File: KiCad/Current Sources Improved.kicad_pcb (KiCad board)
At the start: 4 copper layers, 120 x 75 mm, 97 parts, among them J201 OUT+, J202 OUT-, J203 V+, J204 V-, J301 AVR-ISP-6, J302 USB B, Q201 IRF510, Q401 FMMT614TA, Q402 FMMT734, U201 ADR441, U202 LTC1595, U203 OPA4182, U204 AD7791, U205 ORNTA1001AT1, U301 FT231XS-U, U302 ATMEGA328P-AUR, U303 ADuM261, U304 TMP117xxDRV, U401 L78L15_SOT89, U402 PESE1-S5-S24-M, U403 L78L05, U404 L79L15_SOT89, Y301 16 MHz

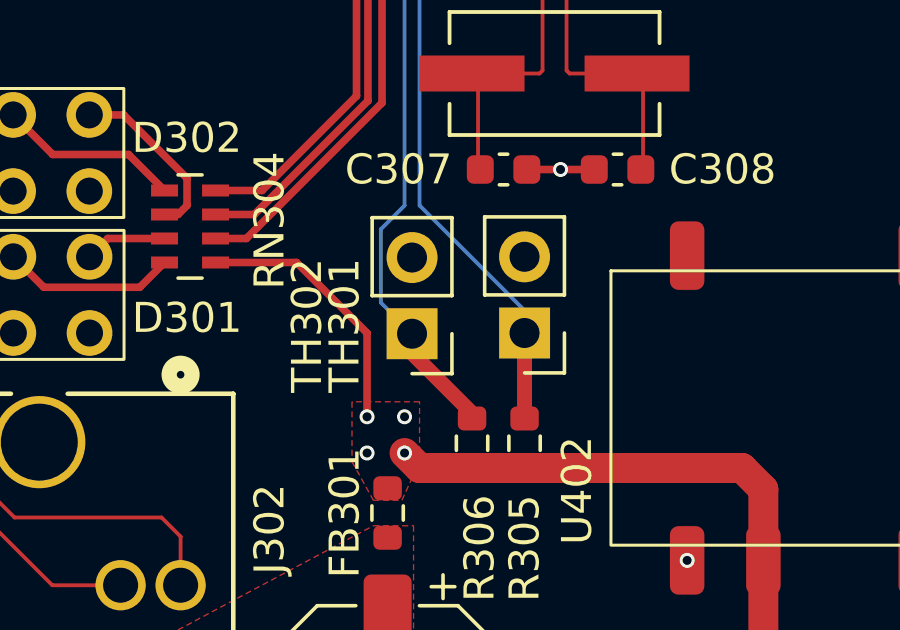
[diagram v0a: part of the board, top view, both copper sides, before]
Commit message: Adjusted designators for NTCs
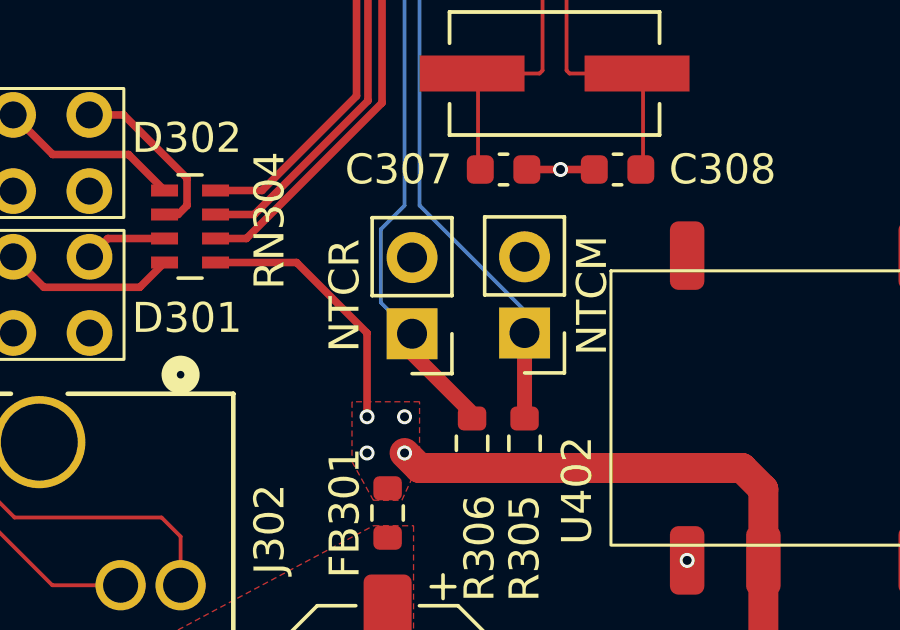
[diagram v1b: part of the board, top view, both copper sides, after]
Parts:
- renumbered TH301 to NTCM, TH302 to NTCR
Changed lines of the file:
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@@
       (drillshape 0)
       (scaleselection 1)
-      (outputdirectory "Z:/Current Sources Improved/Gerbers/")
+      (outputdirectory "Z:/Precision Current Source/KiCad/Gerbers/")
     )
   )
@@
     (property "ki_keywords" "R res thermistor")
     (attr through_hole)
-    (fp_text reference "TH302" (at 3.5 0.275 90) (layer "F.SilkS")
+    (fp_text reference "NTCR" (at 2.25 1.275 90) (layer "F.SilkS")
         (effects (font (size 1 1) (thickness 0.15)))
     )
@@
     (property "ki_keywords" "R res thermistor")
     (attr through_hole)
-    (fp_text reference "TH301" (at 6 0.25 270) (layer "F.SilkS")
+    (fp_text reference "NTCM" (at -2.25 1.25 270) (layer "F.SilkS")
         (effects (font (size 1 1) (thickness 0.15)))
     )
@@
     (effects (font (size 1 1) (thickness 0.15)) (justify left bottom))
   )
-  (gr_text locked "M MORANO\nREV 2.0\n11/27/24" (at 81.5 72) (layer "F.SilkS")
+  (gr_text locked "M MORANO\nREV 2.0\n4/28/25" (at 81.5 72) (layer "F.SilkS")
     (effects (font (size 1 1) (thickness 0.2) bold) (justify left bottom))
   )

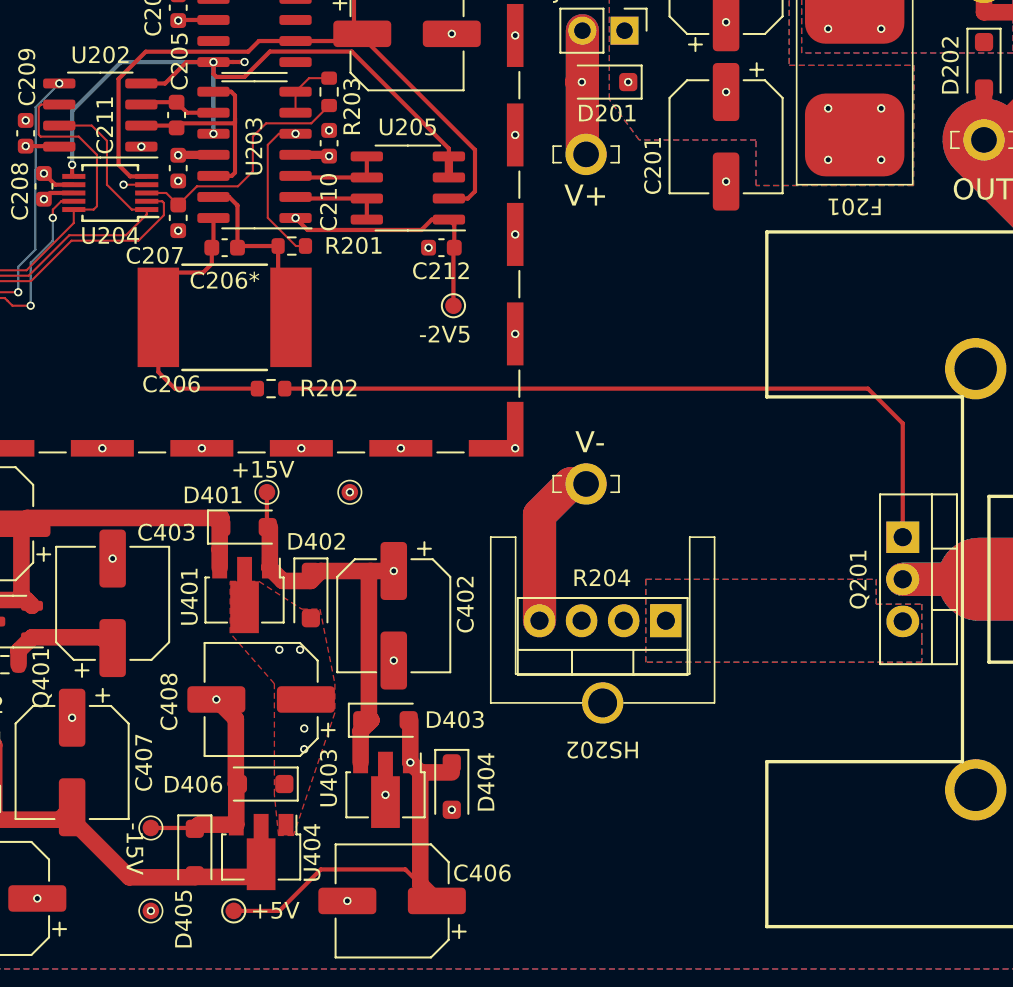
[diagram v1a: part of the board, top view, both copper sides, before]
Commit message: Updated some designators and added component list
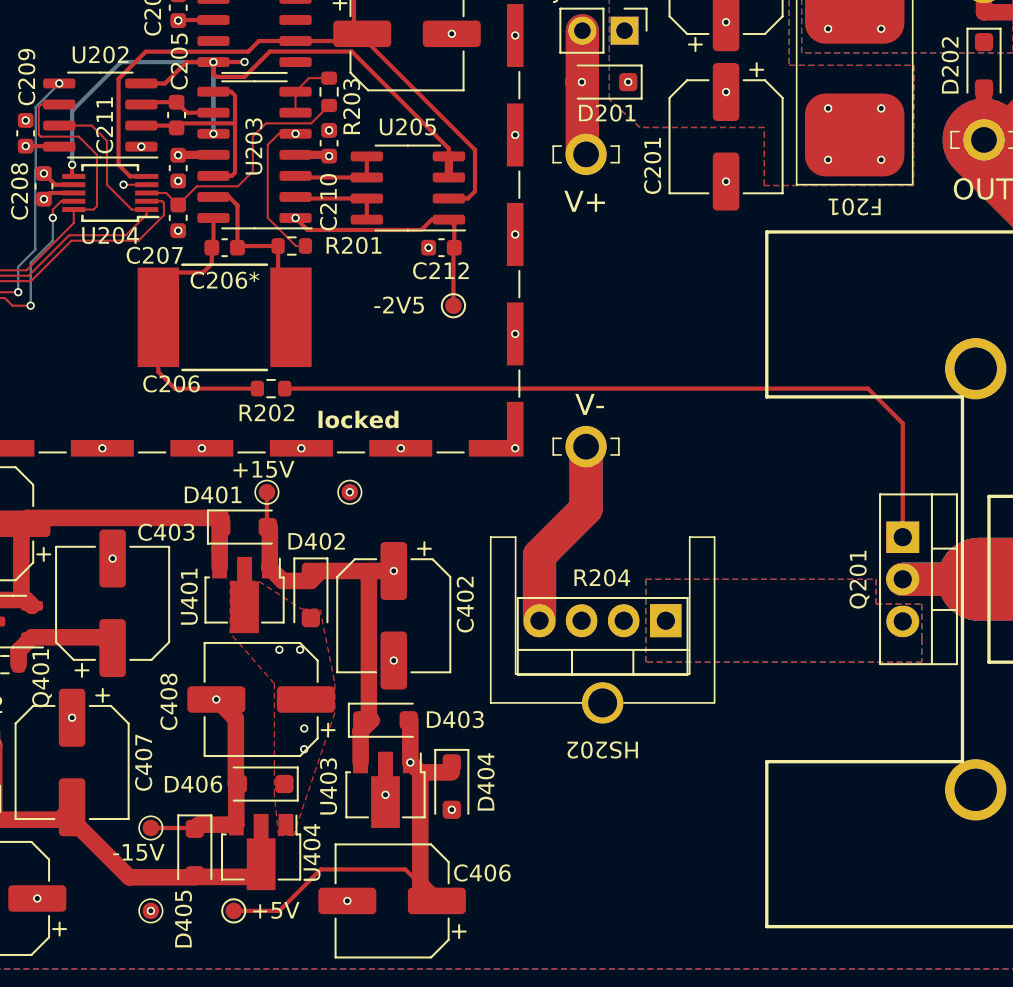
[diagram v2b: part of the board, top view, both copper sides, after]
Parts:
- moved J204 2.25 mm to (162.0, 98.5)
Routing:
- net GNDA: track 28.1 -> 31.5 mm
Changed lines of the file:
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@@
         (effects (font (size 1 1) (thickness 0.1)))
     )
-    (fp_text value "-15V" (at -1.25 1 -90 unlocked) (layer "F.SilkS")
+    (fp_text value "-15V" (at -1 0.75 unlocked) (layer "F.SilkS")
         (effects (font (size 1 1) (thickness 0.15)))
     )
@@
         (effects (font (size 1 1) (thickness 0.15)))
     )
-    (fp_text value "-2V5" (at -0.5 1.75) (layer "F.SilkS")
+    (fp_text value "-2V5" (at -3.25 0) (layer "F.SilkS")
         (effects (font (size 1 1) (thickness 0.15)))
     )
@@
     (property "ki_keywords" "Voltage Regulator 100mA Positive")
     (attr smd)
-    (fp_text reference "U403" (at -1 3.4 90) (layer "F.SilkS")
+    (fp_text reference "U403" (at -0.5 3.4 90) (layer "F.SilkS")
         (effects (font (size 1 1) (thickness 0.15)))
     )
@@
   )
   (footprint "Components:1211" locked (layer "F.Cu")
-    (at 162 100.75 180)
+    (at 162 98.5 180)
     (descr "1211-1")
     (tags "Undefined or Miscellaneous")
@@
         (effects (font (size 1.27 1.27) (thickness 0.254)))
     )
-    (fp_text value "V+" (at 0 2.5) (layer "F.SilkS")
+    (fp_text value "V+" (at 0 2.877596) (layer "F.SilkS")
         (effects (font (size 1.27 1.27) (thickness 0.254)))
     )
@@
     (property "ki_keywords" "R res resistor")
     (attr smd)
-    (fp_text reference "R202" (at 3.5 0) (layer "F.SilkS")
+    (fp_text reference "R202" (at -0.25 1.5) (layer "F.SilkS")
         (effects (font (size 1 1) (thickness 0.15)))
     )
@@
     (effects (font (size 1 1) (thickness 0.2) bold) (justify left bottom))
   )
+  (gr_text locked "DO NOT \nPOPUPLATE\nC206* IF \nUSING C206" (at 145.75 97.5) (layer "F.SilkS")
+    (effects (font (size 1 1) (thickness 0.2) bold) (justify left bottom))
+  )
   (gr_text locked "MOSI" (at 101.75 80.5 90) (layer "F.SilkS")
     (effects (font (size 1 1) (thickness 0.15)) (justify left bottom))
@@
     (style (thickness 0.15) (arrow_length 1.27) (text_position_mode 0) (extension_height 0.58642) (extension_offset 0.5) keep_text_aligned)
   )
+  (segment locked (start 159.19 105.06) (end 159.19 109) (width 2) (layer "F.Cu") (net 1))
   (segment locked (start 141.4 75.3) (end 141.1 75.3) (width 0.254) (layer "F.Cu") (net 1))
-  (segment locked (start 162 100.75) (end 161.05 100.75) (width 2) (layer "F.Cu") (net 1))
-  (segment locked (start 159.19 102.61) (end 159.19 109) (width 2) (layer "F.Cu") (net 1))
-  (segment locked (start 161.05 100.75) (end 159.19 102.61) (width 2) (layer "F.Cu") (net 1))
+  (segment locked (start 162 98.5) (end 162 102.25) (width 2) (layer "F.Cu") (net 1))
+  (segment locked (start 162 102.25) (end 159.19 105.06) (width 2) (layer "F.Cu") (net 1))
   (segment locked (start 129.975 82.7) (end 131.1 82.7) (width 0.254) (layer "F.Cu") (net 1))
   (segment locked (start 119.3 98.7) (end 119.3 99.90625) (width 1) (layer "F.Cu") (net 1))
@@
   (via locked (at 114.54 119.83) (size 0.5) (drill 0.3) (layers "F.Cu" "B.Cu") (net 1))
   (via locked (at 157.725 66.8) (size 0.5) (drill 0.3) (layers "F.Cu" "B.Cu") (net 1))
-  (segment locked (start 161.05 100.75) (end 159.19 102.61) (width 2) (layer "B.Cu") (net 1))
-  (segment locked (start 162 100.75) (end 161.05 100.75) (width 2) (layer "B.Cu") (net 1))
-  (segment locked (start 159.19 102.61) (end 159.19 109) (width 2) (layer "B.Cu") (net 1))
+  (segment locked (start 159.19 105.06) (end 159.19 109) (width 2) (layer "B.Cu") (net 1))
+  (segment locked (start 162 102.25) (end 159.19 105.06) (width 2) (layer "B.Cu") (net 1))
+  (segment locked (start 162 98.5) (end 162 102.25) (width 2) (layer "B.Cu") (net 1))
   (segment locked (start 84.5095 91.5095) (end 84.9406 91.9406) (width 0.127) (layer "F.Cu") (net 3))
   (segment locked (start 88.0351 120.657901) (end 85.757901 120.657901) (width 0.127) (layer "F.Cu") (net 3))
@@
         (xy 181.775 75.5)
         (xy 181.75 82.75)
-        (xy 172.25 82.75)
-        (xy 172.25 80)
-        (xy 165.2 80)
+        (xy 172.75 82.75)
+        (xy 172.75 79.25)
+        (xy 165.25 79.25)
         (xy 163.4 77.560663)
       )
@@
     (polygon
       (pts
-        (xy 159.4 69.3)
+        (xy 159 69.3)
         (xy 171.3 69.3)
         (xy 171.3 65.4)
@@
         (xy 171.3 85.8)
         (xy 171.3 80.7)
-        (xy 165.2 80.7)
-        (xy 165.2 82.7)
-        (xy 159.4 82.7)
+        (xy 166 80.7)
+        (xy 166 83.5)
+        (xy 159 83.5)
       )
     )

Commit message: Cleaned up a few things
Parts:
- renumbered NTCR to TH301, NTCM to TH302
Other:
- board text added: "NTCM"
- board text added: "NTCR"
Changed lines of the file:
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@@
     (property "ki_keywords" "R res thermistor")
     (attr through_hole)
-    (fp_text reference "NTCR" (at 2.25 1.275 90) (layer "F.SilkS")
+    (fp_text reference "TH301" (at 2.25 1.275 90) (layer "F.SilkS") hide
         (effects (font (size 1 1) (thickness 0.15)))
     )
@@
     (property "ki_keywords" "R res thermistor")
     (attr through_hole)
-    (fp_text reference "NTCM" (at -2.25 1.25 270) (layer "F.SilkS")
+    (fp_text reference "TH302" (at -2.25 1.25 270) (layer "F.SilkS") hide
         (effects (font (size 1 1) (thickness 0.15)))
     )
@@
   (gr_rect locked (start 80 60) (end 200 135)
     (stroke (width 0.1) (type default)) (fill none) (layer "Edge.Cuts"))
+  (gr_text "NTCR" (at 95.5 110.75 90) (layer "F.SilkS")
+    (effects (font (size 1 1) (thickness 0.15)))
+  )
   (gr_text locked "GND" (at 99.25 80.25 90) (layer "F.SilkS")
     (effects (font (size 1 1) (thickness 0.15)) (justify left bottom))
@@
     (effects (font (size 1 1) (thickness 0.15)) (justify left bottom))
   )
+  (gr_text "NTCM" (at 103.75 110.75 90) (layer "F.SilkS")
+    (effects (font (size 1 1) (thickness 0.15)))
+  )
   (gr_text locked "M MORANO\nREV 2.0\n4/28/25" (at 81.5 72) (layer "F.SilkS")
